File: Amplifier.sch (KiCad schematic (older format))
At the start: 50 parts

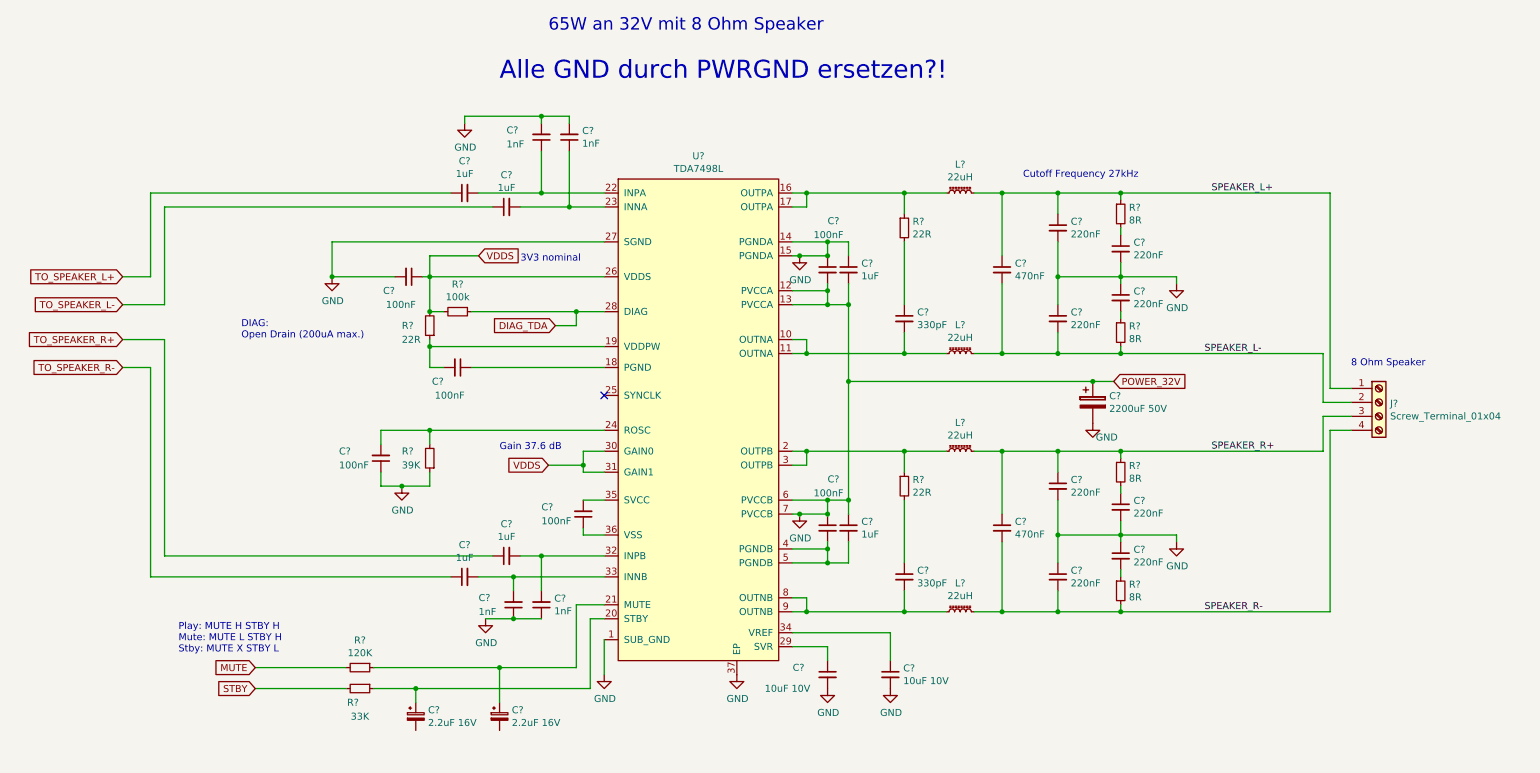
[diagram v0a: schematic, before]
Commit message: LDO für Audio DSP hinzugefügt
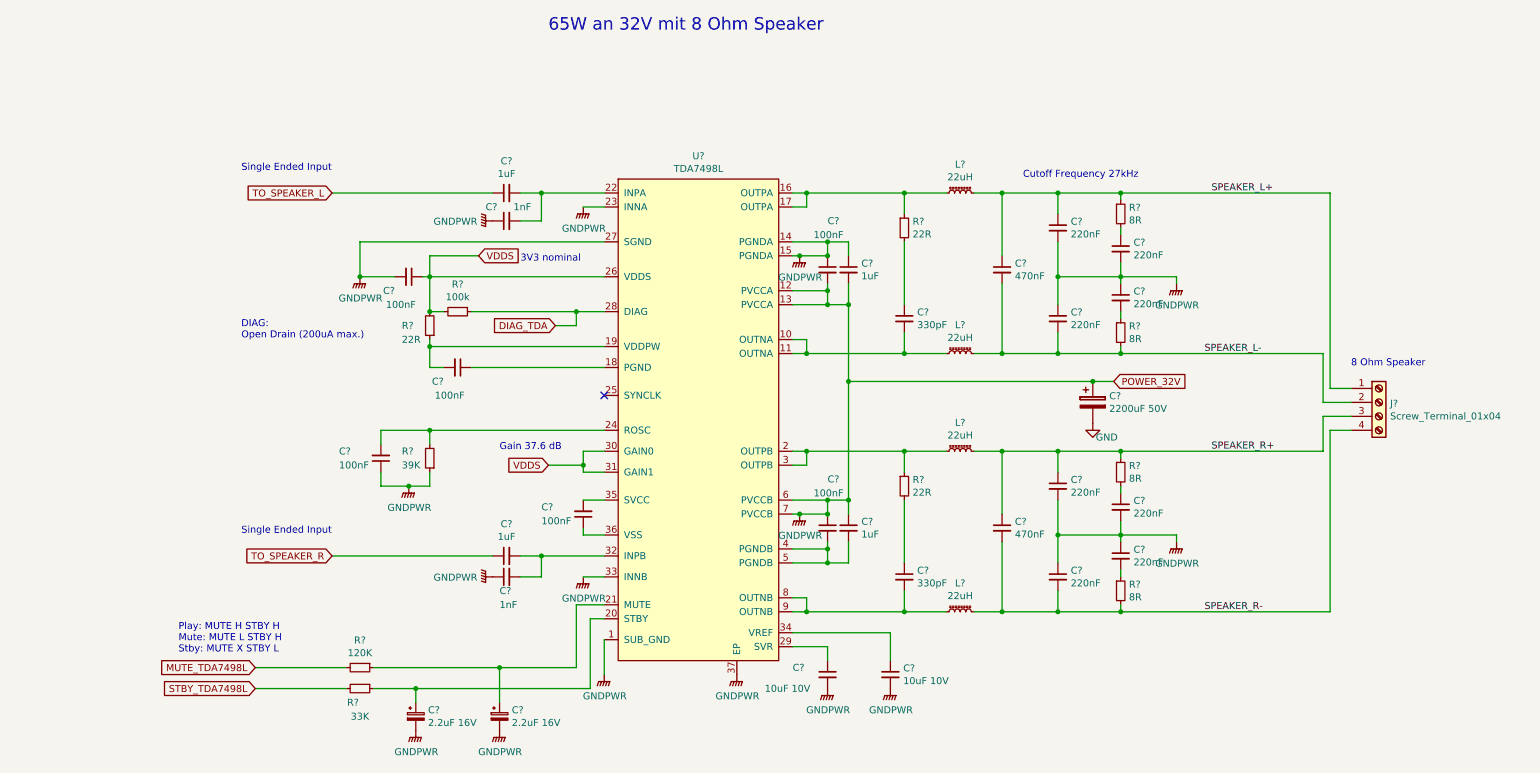
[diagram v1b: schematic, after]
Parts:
- removed C? (x2): 1uF, symbol Device:C_Small
- removed C? (x2): 1nF, symbol Device:C_Small
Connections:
- net GND: no longer C?.1, C?.1, C?.1, C?.1, C?.1, C?.1, C?.1, C?.1, C?.1, C?.1, C?.1, C?.2, C?.2, C?.2, C?.2, C?.2, C?.2, C?.2, C?.2, C?.2, C?.2, R?.1, U?.1 (SUB_GND), U?.12 (PVCCA), U?.13 (PVCCA), U?.14 (PGNDA), U?.15 (PGNDA), U?.27 (SGND), U?.37 (EP), U?.6 (PVCCB), U?.7 (PVCCB)
- net at C?.2, U?.22 (INPA): now also C?.2; no longer C?.1
- net GNDPWR: now reaches U?.23 (INNA)
- net GNDPWR: now also C?.1, C?.1, C?.1, C?.1, C?.1, C?.1, C?.1, C?.1, C?.1, C?.1, C?.1, C?.1, C?.2, C?.2, C?.2, C?.2, C?.2, C?.2, C?.2, C?.2, C?.2, C?.2, C?.2, R?.1, U?.1 (SUB_GND), U?.12 (PVCCA), U?.13 (PVCCA), U?.14 (PGNDA), U?.15 (PGNDA), U?.27 (SGND), U?.33 (INNB), U?.37 (EP), U?.6 (PVCCB), U?.7 (PVCCB)
- net MUTE renamed MUTE_TDA7498L
- net STBY renamed STBY_TDA7498L
- net TO_SPEAKER_L+ renamed TO_SPEAKER_L
- net TO_SPEAKER_R+ renamed TO_SPEAKER_R
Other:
- note added: "Single Ended Input"
- note removed: "Alle GND durch PWRGND ersetzen?!"
- moved on the sheet: C?

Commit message: 3v3 über LDO von BMS enablen. Bluetooth hinzugefügt
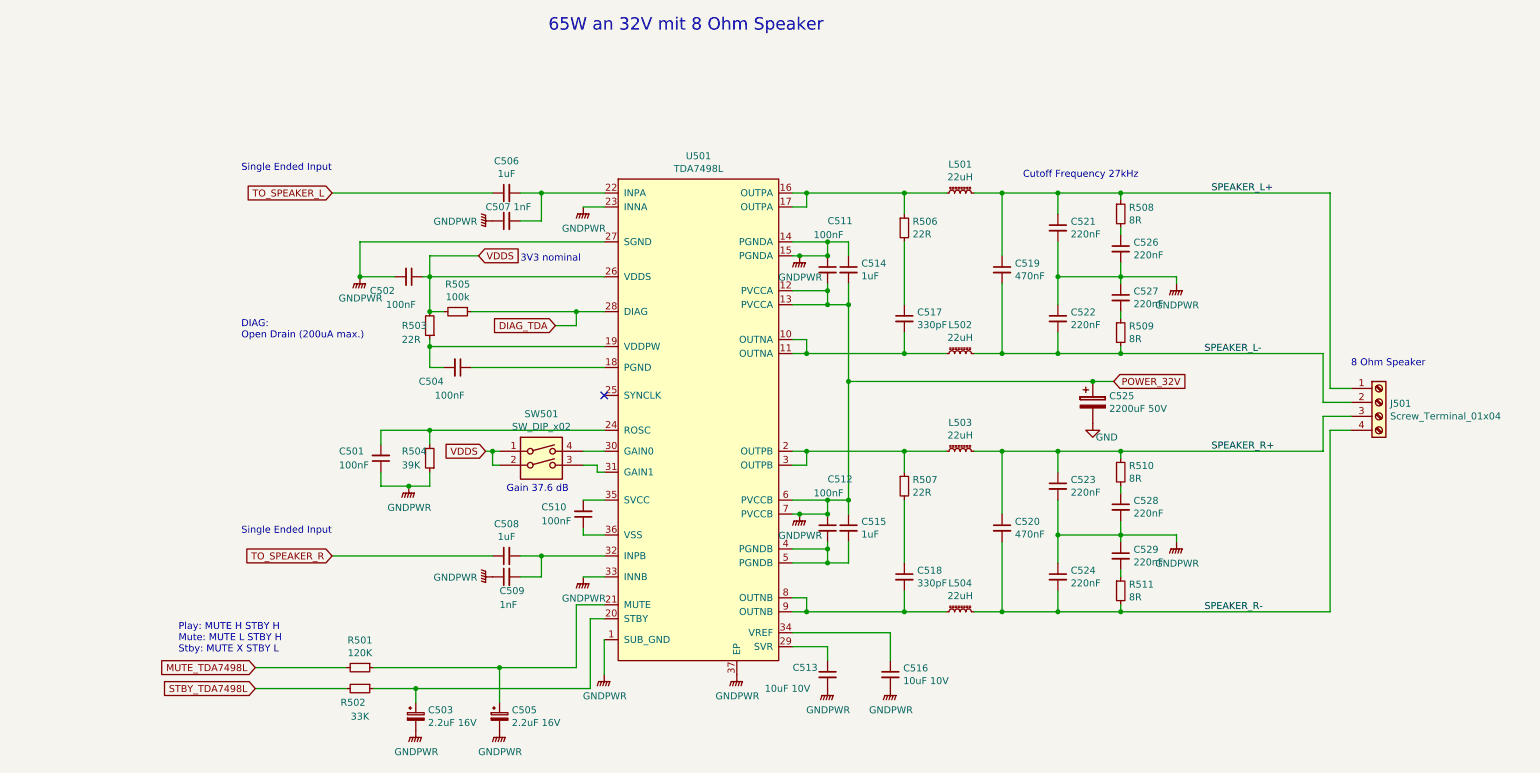
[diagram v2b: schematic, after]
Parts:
- added SW501: SW_DIP_x02, symbol Switch:SW_DIP_x02
- gave numbers to parts that had none: 46
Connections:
- net VDDS: now also SW501.1, SW501.2; no longer U501.30 (GAIN0), U501.31 (GAIN1)
- new net: SW501.4, U501.30 (GAIN0)
- new net: SW501.3, U501.31 (GAIN1)

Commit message: power schalter und taser hinzugefügt. Selbsthaltung LDO hinzugefügt. Gain Potis hinzugefügt, Separater Ground für Audio Lines
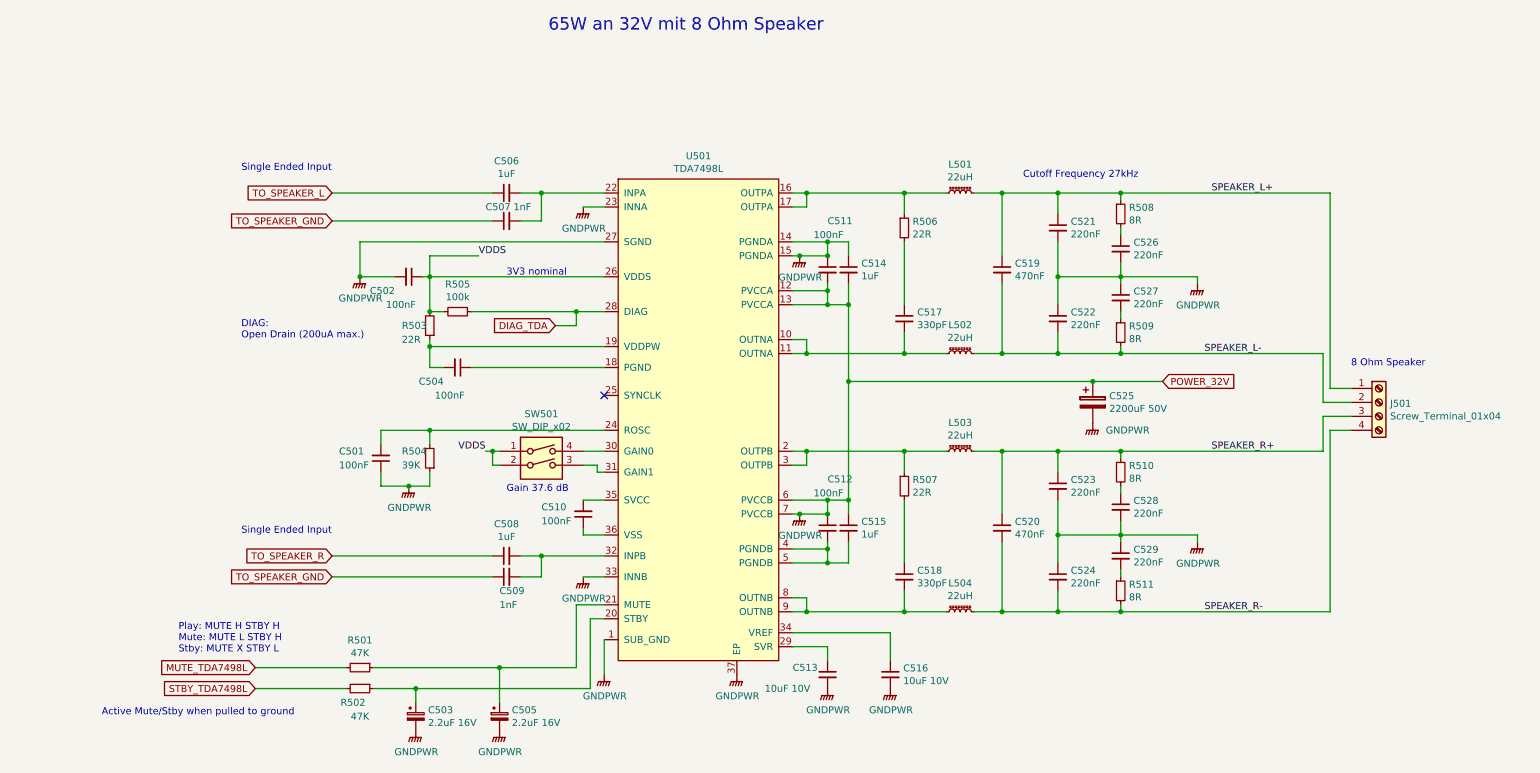
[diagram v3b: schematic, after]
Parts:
- R501: value 120K -> 47K
- R502: value 33K -> 47K
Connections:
- net GND is gone; now on net GNDPWR: C525.2
- net GNDPWR: no longer C507.1, C509.1
- new net TO_SPEAKER_GND: C507.1, C509.1
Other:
- note added: "Active Mute/Stby when pulled to ground"
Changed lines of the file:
@@
 	8450 2750 8450 2650
 Wire Wire Line
-	8850 2800 8850 2750
-Wire Wire Line
-	8850 2750 8450 2750
+	9000 2800 9000 2750
+Wire Wire Line
+	9000 2750 8450 2750
 $Comp
 L Connector:Screw_Terminal_01x04 J501
@@
 	8450 4600 8450 4500
 Wire Wire Line
-	8850 4650 8850 4600
-Wire Wire Line
-	8850 4600 8450 4600
+	9000 4650 9000 4600
+Wire Wire Line
+	9000 4600 8450 4600
 Connection ~ 8450 4000
 Connection ~ 8450 5150
@@
 Wire Wire Line
 	8450 3300 9900 3300
-Text GLabel 8400 3500 2    50   Input ~ 0
+Text GLabel 8750 3500 2    50   Input ~ 0
 POWER_32V
 $Comp
@@
 	1    0    0    -1
 $EndComp
-$Comp
-L power:GND #PWR0142
-U 1 1 5E78AB60
-P 8250 3800
-F 0 "#PWR0142" H 8250 3550 50  0001 C CNN
-F 1 "GND" H 8350 3700 50  0000 C CNN
-F 2 "" H 8250 3800 50  0001 C CNN
-F 3 "" H 8250 3800 50  0001 C CNN
-	1    8250 3800
-	1    0    0    -1
-$EndComp
-Wire Wire Line
-	8400 3500 8250 3500
+Wire Wire Line
+	8750 3500 8250 3500
 Wire Wire Line
 	8250 3500 6500 3500
@@
 Wire Wire Line
 	4750 3000 4550 3000
-Text GLabel 3850 2600 2    50   Input ~ 0
-VDDS
 Wire Wire Line
 	3850 2600 3500 2600
@@
 Wire Wire Line
 	4550 3000 3800 3000
-Text Notes 4150 2650 0    50   ~ 0
+Text Notes 4050 2750 0    50   ~ 0
 3V3 nominal
 $Comp
@@
 Wire Wire Line
 	3800 3400 4750 3400
-Text GLabel 3900 4000 0    50   Input ~ 0
-VDDS
 $Comp
 L Device:C_Small C501
@@
 P 3000 5700
 F 0 "R502" V 3100 5650 50  0000 C CNN
-F 1 "33K" V 3200 5700 50  0000 C CNN
+F 1 "47K" V 3200 5700 50  0000 C CNN
 F 2 "" H 3000 5700 50  0001 C CNN
 F 3 "~" H 3000 5700 50  0001 C CNN
@@
 P 3000 5550
 F 0 "R501" V 2804 5550 50  0000 C CNN
-F 1 "120K" V 2895 5550 50  0000 C CNN
+F 1 "47K" V 2895 5550 50  0000 C CNN
 F 2 "" H 3000 5550 50  0001 C CNN
 F 3 "~" H 3000 5550 50  0001 C CNN
@@
 L power:GNDPWR #PWR0149
 U 1 1 5EA56B3F
-P 8850 2800
-F 0 "#PWR0149" H 8850 2600 50  0001 C CNN
-F 1 "GNDPWR" H 8854 2646 50  0000 C CNN
-F 2 "" H 8850 2750 50  0001 C CNN
-F 3 "" H 8850 2750 50  0001 C CNN
-	1    8850 2800
+P 9000 2800
+F 0 "#PWR0149" H 9000 2600 50  0001 C CNN
+F 1 "GNDPWR" H 9004 2646 50  0000 C CNN
+F 2 "" H 9000 2750 50  0001 C CNN
+F 3 "" H 9000 2750 50  0001 C CNN
+	1    9000 2800
 	1    0    0    -1
 $EndComp
@@
 L power:GNDPWR #PWR0150
 U 1 1 5EA56C81
-P 8850 4650
-F 0 "#PWR0150" H 8850 4450 50  0001 C CNN
-F 1 "GNDPWR" H 8854 4496 50  0000 C CNN
-F 2 "" H 8850 4600 50  0001 C CNN
-F 3 "" H 8850 4600 50  0001 C CNN
-	1    8850 4650
+P 9000 4650
+F 0 "#PWR0150" H 9000 4450 50  0001 C CNN
+F 1 "GNDPWR" H 9004 4496 50  0000 C CNN
+F 2 "" H 9000 4600 50  0001 C CNN
+F 3 "" H 9000 4600 50  0001 C CNN
+	1    9000 4650
 	1    0    0    -1
 $EndComp
@@
 $EndComp
 $Comp
-L power:GNDPWR #PWR0153
-U 1 1 5EA57139
-P 3950 4900
-F 0 "#PWR0153" H 3950 4700 50  0001 C CNN
-F 1 "GNDPWR" V 3954 4791 50  0000 R CNN
-F 2 "" H 3950 4850 50  0001 C CNN
-F 3 "" H 3950 4850 50  0001 C CNN
-	1    3950 4900
-	0    1    1    0
-$EndComp
-$Comp
 L power:GNDPWR #PWR0154
 U 1 1 5EA574FA
@@
 $EndComp
 $Comp
-L power:GNDPWR #PWR0156
-U 1 1 5EA579EA
-P 3950 2350
-F 0 "#PWR0156" H 3950 2150 50  0001 C CNN
-F 1 "GNDPWR" V 3954 2241 50  0000 R CNN
-F 2 "" H 3950 2300 50  0001 C CNN
-F 3 "" H 3950 2300 50  0001 C CNN
-	1    3950 2350
-	0    1    1    0
-$EndComp
-$Comp
 L power:GNDPWR #PWR0157
 U 1 1 5EA781BB
@@
 Wire Wire Line
 	4700 4100 4600 4100
+Text Label 3850 2600 0    50   ~ 0
+VDDS
+Text Label 3900 4000 2    50   ~ 0
+VDDS
+$Comp
+L power:GNDPWR #PWR?
+U 1 1 5E90BDCB
+P 8250 3800
+F 0 "#PWR?" H 8250 3600 50  0001 C CNN
+F 1 "GNDPWR" H 8500 3750 50  0000 C CNN
+F 2 "" H 8250 3750 50  0001 C CNN
+F 3 "" H 8250 3750 50  0001 C CNN
+	1    8250 3800
+	1    0    0    -1
+$EndComp
+Text Notes 1150 5900 0    50   ~ 0
+Active Mute/Stby when pulled to ground
+Text GLabel 2800 4900 0    50   Input ~ 0
+TO_SPEAKER_GND
+Wire Wire Line
+	3950 4900 2800 4900
+Text GLabel 2800 2350 0    50   Input ~ 0
+TO_SPEAKER_GND
+Wire Wire Line
+	3950 2350 2800 2350
 $EndSCHEMATC

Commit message: Schaltplan fertig. Fertig für review
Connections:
- net GNDPWR: no longer U501.23 (INNA), U501.33 (INNB)
- net DIAG_TDA renamed DIAG_TDA7598
- net MUTE_TDA7498L renamed MUTE_TDA7498
- net STBY_TDA7498L renamed STBY_TDA7498
- net TO_SPEAKER_GND renamed GNDA
- net GNDA: now also U501.23 (INNA), U501.33 (INNB)
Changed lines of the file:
@@
 	3500 3000 3600 3000
 Text GLabel 4400 3100 0    50   Input ~ 0
-DIAG_TDA
+DIAG_TDA7598
 Wire Wire Line
 	4400 3100 4550 3100
@@
 65W an 32V mit 8 Ohm Speaker
 Text GLabel 2250 5550 0    50   Input ~ 0
-MUTE_TDA7498L
+MUTE_TDA7498
 Text GLabel 2250 5700 0    50   Input ~ 0
-STBY_TDA7498L
+STBY_TDA7498
 Wire Wire Line
 	2900 5550 2250 5550
@@
 	1    0    0    -1
 $EndComp
-$Comp
-L power:GNDPWR #PWR0157
-U 1 1 5EA781BB
-P 4600 2250
-F 0 "#PWR0157" H 4600 2050 50  0001 C CNN
-F 1 "GNDPWR" H 4604 2096 50  0000 C CNN
-F 2 "" H 4600 2200 50  0001 C CNN
-F 3 "" H 4600 2200 50  0001 C CNN
-	1    4600 2250
-	1    0    0    -1
-$EndComp
 Wire Wire Line
 	4600 2250 4750 2250
@@
 Wire Wire Line
 	4300 2150 4750 2150
-$Comp
-L power:GNDPWR #PWR0158
-U 1 1 5EAA15BD
-P 4600 4900
-F 0 "#PWR0158" H 4600 4700 50  0001 C CNN
-F 1 "GNDPWR" H 4604 4746 50  0000 C CNN
-F 2 "" H 4600 4850 50  0001 C CNN
-F 3 "" H 4600 4850 50  0001 C CNN
-	1    4600 4900
-	1    0    0    -1
-$EndComp
-Wire Wire Line
-	4600 4900 4750 4900
+Wire Wire Line
+	4400 4900 4750 4900
 Wire Wire Line
 	4150 4900 4300 4900
@@
 Text Notes 1150 5900 0    50   ~ 0
 Active Mute/Stby when pulled to ground
-Text GLabel 2800 4900 0    50   Input ~ 0
-TO_SPEAKER_GND
-Wire Wire Line
-	3950 4900 2800 4900
-Text GLabel 2800 2350 0    50   Input ~ 0
-TO_SPEAKER_GND
-Wire Wire Line
-	3950 2350 2800 2350
+$Comp
+L power:GNDA #PWR?
+U 1 1 5E90FE70
+P 4600 2250
+F 0 "#PWR?" H 4600 2000 50  0001 C CNN
+F 1 "GNDA" H 4605 2077 50  0000 C CNN
+F 2 "" H 4600 2250 50  0001 C CNN
+F 3 "" H 4600 2250 50  0001 C CNN
+	1    4600 2250
+	1    0    0    -1
+$EndComp
+$Comp
+L power:GNDA #PWR?
+U 1 1 5E90FF3E
+P 3950 2350
+F 0 "#PWR?" H 3950 2100 50  0001 C CNN
+F 1 "GNDA" V 3955 2223 50  0000 R CNN
+F 2 "" H 3950 2350 50  0001 C CNN
+F 3 "" H 3950 2350 50  0001 C CNN
+	1    3950 2350
+	0    1    1    0
+$EndComp
+$Comp
+L power:GNDA #PWR?
+U 1 1 5E9101AD
+P 4400 4900
+F 0 "#PWR?" H 4400 4650 50  0001 C CNN
+F 1 "GNDA" H 4405 4727 50  0000 C CNN
+F 2 "" H 4400 4900 50  0001 C CNN
+F 3 "" H 4400 4900 50  0001 C CNN
+	1    4400 4900
+	1    0    0    -1
+$EndComp
+$Comp
+L power:GNDA #PWR?
+U 1 1 5E910245
+P 3950 4900
+F 0 "#PWR?" H 3950 4650 50  0001 C CNN
+F 1 "GNDA" V 3955 4773 50  0000 R CNN
+F 2 "" H 3950 4900 50  0001 C CNN
+F 3 "" H 3950 4900 50  0001 C CNN
+	1    3950 4900
+	0    1    1    0
+$EndComp
 $EndSCHEMATC

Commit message: Footprintzuordnung angefangen
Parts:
- added C?: 560uF 50V, symbol Device:CP_Small
- added R512: 0R, symbol Device:R_Small
- C501, C502, C504, C506, C507, C508, C509, C510, C511, C512, C513, C514, C515, C516, C517, C518, C519, C520, C521, C522, C523, C524: footprint (none) -> Capacitor_SMD:C_0603_1608Metric_Pad1.05x0.95mm_HandSolder
- C503, C505: footprint (none) -> Capacitor_SMD:CP_Elec_4x5.4
- C525: value 2200uF 50V -> 560uF 50V; footprint (none) -> Capacitor_THT:CP_Radial_D12.5mm_P5.00mm
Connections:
- net GNDA: now also C507.2, C509.2; no longer C507.1, C509.1
- net GNDPWR: now also C512.2, C515.2, U501.4 (PGNDB), U501.5 (PGNDB), R512.1; no longer C501.1, C502.2, C503.2, C505.2, C511.2, C512.1, C513.2, C514.2, C515.1, C516.2, C525.1, R504.1, U501.12 (PVCCA), U501.13 (PVCCA), U501.27 (SGND), U501.6 (PVCCB), U501.7 (PVCCB)
- net at C506.2, U501.22 (INPA): now also C507.1; no longer C507.2
- net at C508.2, U501.32 (INPB): now also C509.1; no longer C509.2
- net DIAG_TDA7598 renamed DIAG_TDA7498
- new net: C511.2, C512.1, C514.2, C515.1, C525.1, U501.12 (PVCCA), U501.13 (PVCCA), U501.6 (PVCCB), U501.7 (PVCCB)
- new net GNDS: C501.1, C502.2, C503.2, C505.2, C513.2, C516.2, R504.1, R512.2, U501.27 (SGND)
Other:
- moved on the sheet: C507, C509
